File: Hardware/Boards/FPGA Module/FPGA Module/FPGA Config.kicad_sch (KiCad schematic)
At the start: 37 parts, among them Q1 IRLML6244, SW2 RST, SW3 SW_DIP_x03, U1 XCKU3P-FFVA676, U11 MT25QUxxxxxx1xW7, U19 MAX6070BAUT12V+T

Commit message: Completed FPGA module PCB layout
Started PCB routing
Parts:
- C119: renamed from C42; value 4.7uF -> 100nF; footprint Capacitor_SMD:C_0402_1005Metric -> Capacitor_SMD:C_0201_0603Metric
- C120: renamed from C56; footprint Capacitor_SMD:C_0402_1005Metric -> Capacitor_SMD:C_0201_0603Metric
- C121: renamed from C43; footprint Capacitor_SMD:C_0402_1005Metric -> Capacitor_SMD:C_0201_0603Metric
- C122: renamed from C44; footprint Capacitor_SMD:C_0402_1005Metric -> Capacitor_SMD:C_0201_0603Metric
- C123: renamed from C45; footprint Capacitor_SMD:C_0402_1005Metric -> Capacitor_SMD:C_0201_0603Metric
- C124: renamed from C57; footprint Capacitor_SMD:C_0402_1005Metric -> Capacitor_SMD:C_0201_0603Metric
- FB1: footprint (none) -> Inductor_SMD:L_0201_0603Metric
- FB2: renamed from FB3; footprint (none) -> Inductor_SMD:L_0201_0603Metric
- FB3: renamed from FB4; footprint (none) -> Inductor_SMD:L_0201_0603Metric
- R108: renamed from R25; footprint Resistor_SMD:R_0402_1005Metric -> Resistor_SMD:R_0201_0603Metric
- R109: renamed from R26; footprint Resistor_SMD:R_0402_1005Metric -> Resistor_SMD:R_0201_0603Metric
- R110: renamed from R27; footprint Resistor_SMD:R_0402_1005Metric -> Resistor_SMD:R_0201_0603Metric
- R111: renamed from R28; footprint Resistor_SMD:R_0402_1005Metric -> Resistor_SMD:R_0201_0603Metric
- R112: renamed from R51; footprint Resistor_SMD:R_0402_1005Metric -> Resistor_SMD:R_0201_0603Metric
- R113: renamed from R50; footprint Resistor_SMD:R_0402_1005Metric -> Resistor_SMD:R_0201_0603Metric
- R114: renamed from R49; footprint Resistor_SMD:R_0402_1005Metric -> Resistor_SMD:R_0201_0603Metric
- R115: renamed from R58; footprint Resistor_SMD:R_0402_1005Metric -> Resistor_SMD:R_0201_0603Metric
- R116: renamed from R59; footprint Resistor_SMD:R_0402_1005Metric -> Resistor_SMD:R_0201_0603Metric
- R117: renamed from R60; footprint Resistor_SMD:R_0402_1005Metric -> Resistor_SMD:R_0201_0603Metric
- R118: renamed from R52; footprint Resistor_SMD:R_0402_1005Metric -> Resistor_SMD:R_0201_0603Metric
- R119: renamed from R81; footprint Resistor_SMD:R_0402_1005Metric -> Resistor_SMD:R_0201_0603Metric
- R120: renamed from R57; footprint Resistor_SMD:R_0402_1005Metric -> Resistor_SMD:R_0201_0603Metric
- R121: renamed from R53; footprint Resistor_SMD:R_0402_1005Metric -> Resistor_SMD:R_0201_0603Metric
- R122: renamed from R55; footprint Resistor_SMD:R_0402_1005Metric -> Resistor_SMD:R_0201_0603Metric
- R123: renamed from R61; footprint Resistor_SMD:R_0402_1005Metric -> Resistor_SMD:R_0201_0603Metric; now fitted
- R124: renamed from R54; footprint Resistor_SMD:R_0402_1005Metric -> Resistor_SMD:R_0201_0603Metric; now fitted
- R125: renamed from R56; footprint Resistor_SMD:R_0402_1005Metric -> Resistor_SMD:R_0201_0603Metric; now fitted
- R126: renamed from R62; footprint Resistor_SMD:R_0402_1005Metric -> Resistor_SMD:R_0201_0603Metric
- renumbered D8 to D12, Q1 to Q10, TP46 to TP50, TP47 to TP51, U11 to U20, U19 to U21
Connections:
- net FPGA_VREF_N: now also C122.2
- net GND: no longer C119.2, C122.2
- net GNDADC: now reaches FB2.1, U1.N11 (GNDADC)
- net GNDADC: now also C119.2
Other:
- moved on the sheet: C122, FB2

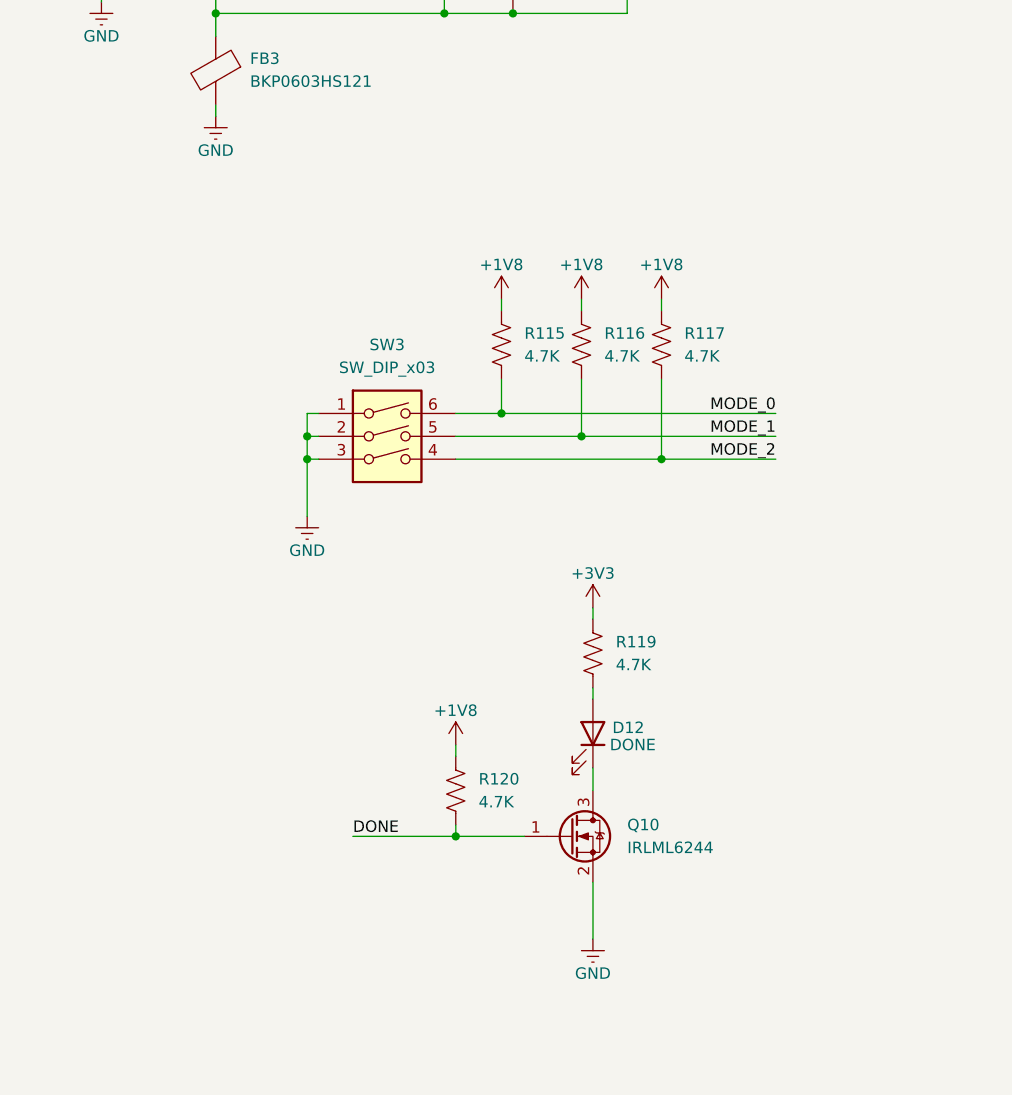
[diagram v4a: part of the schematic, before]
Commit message: Updated SCH and Layout
Added temp sensors for DCDC's, Added MCU control for FPGA mode, removed mode DIP switch
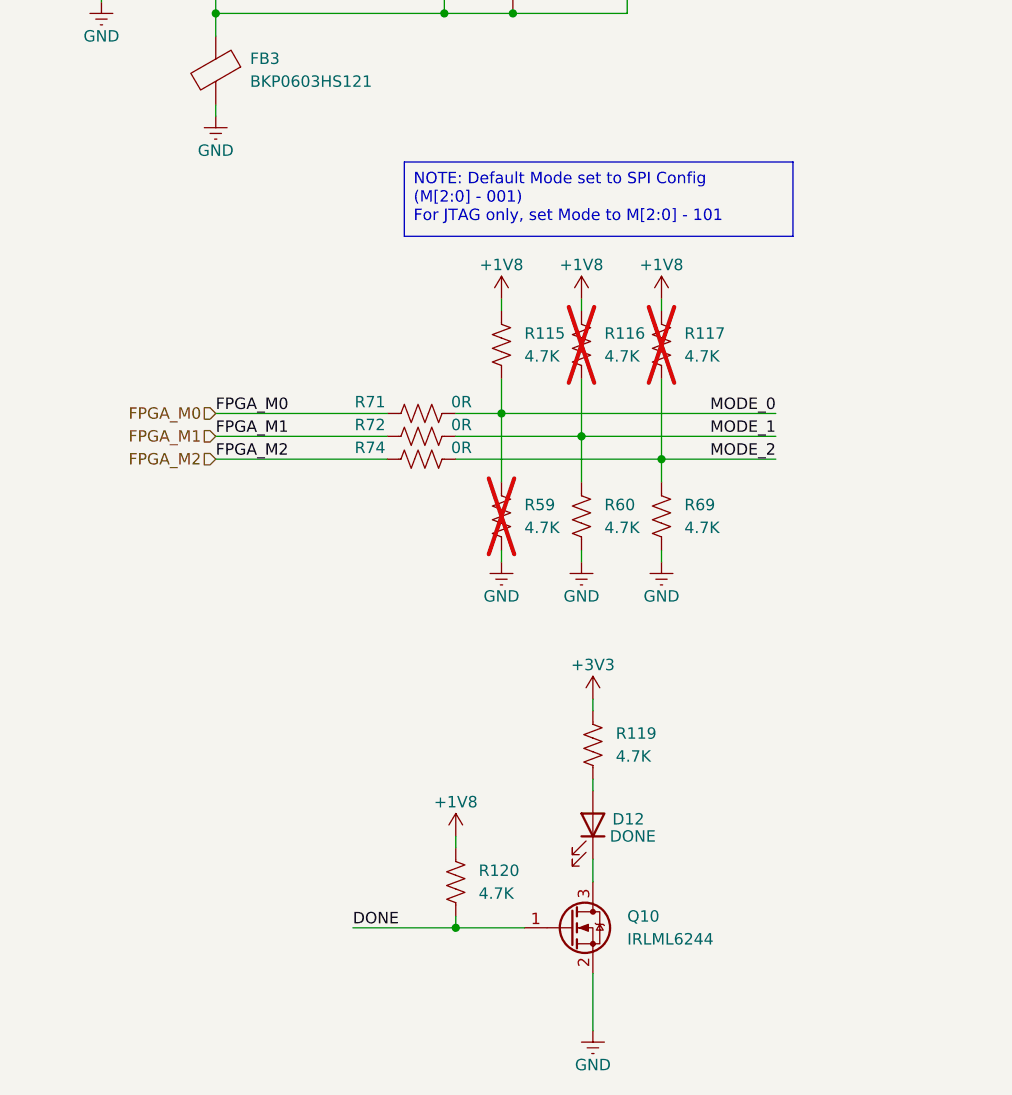
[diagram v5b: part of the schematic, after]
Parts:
- removed SW3: SW_DIP_x03, Button_Switch_SMD:SW_DIP_SPSTx03_Slide_KingTek_DSHP03TJ_W5.25mm_P1.27mm_JPin, symbol Switch:SW_DIP_x03
- added R59, R60, R69: 4.7K, Resistor_SMD:R_0201_0603Metric, symbol Device:R_US
- added R71, R72, R74: 0R, Resistor_SMD:R_0201_0603Metric, symbol Device:R_US
- R116, R117: now not fitted
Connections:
- net GND: now also R59.1, R60.1, R69.1
- net MODE_0: now also R59.2, R71.1
- net MODE_1: now also R60.2, R72.1
- net MODE_2: now also R69.2, R74.1
- new net FPGA_M0: R71.2
- new net FPGA_M1: R72.2
- new net FPGA_M2: R74.2
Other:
- moved on the sheet: D12, Q10, R119, R120

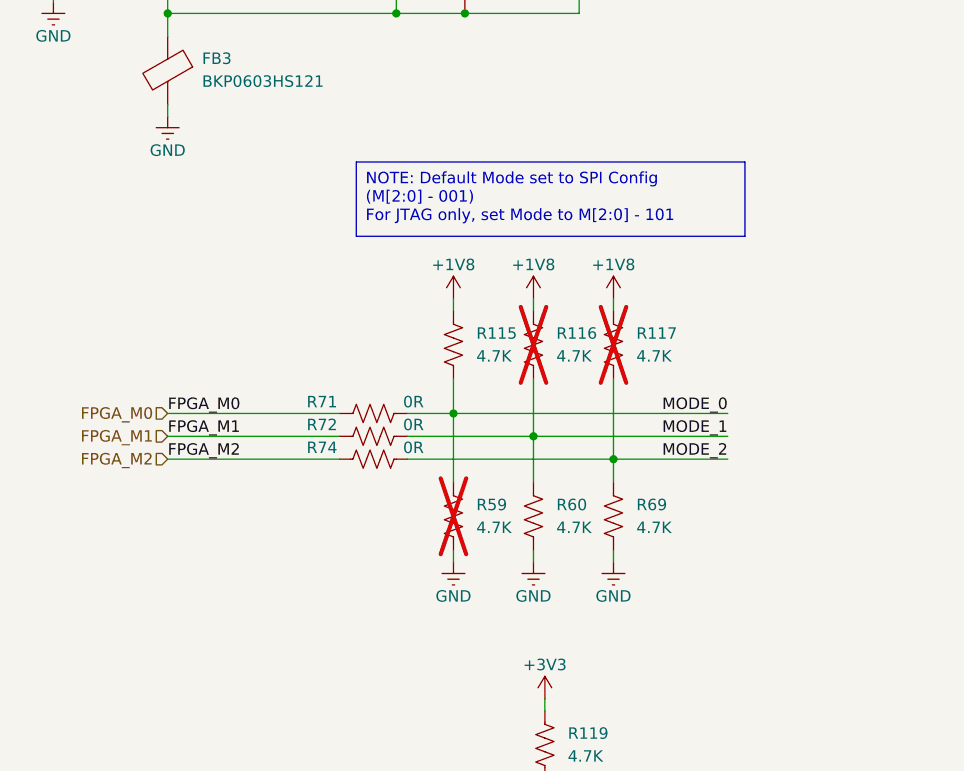
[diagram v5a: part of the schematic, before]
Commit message: FPGA Layout update
Added power panes & moved IO Buffer to MCU
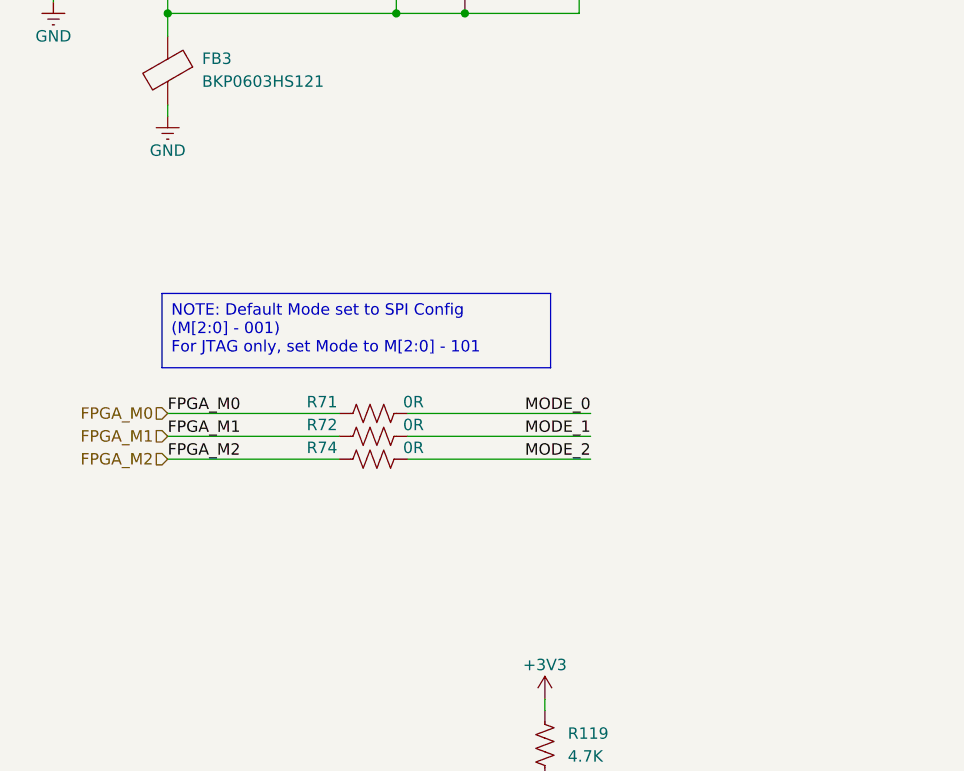
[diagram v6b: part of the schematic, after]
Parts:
- removed R115, R116, R117, R59, R60, R69: 4.7K, Resistor_SMD:R_0201_0603Metric, symbol Device:R_US

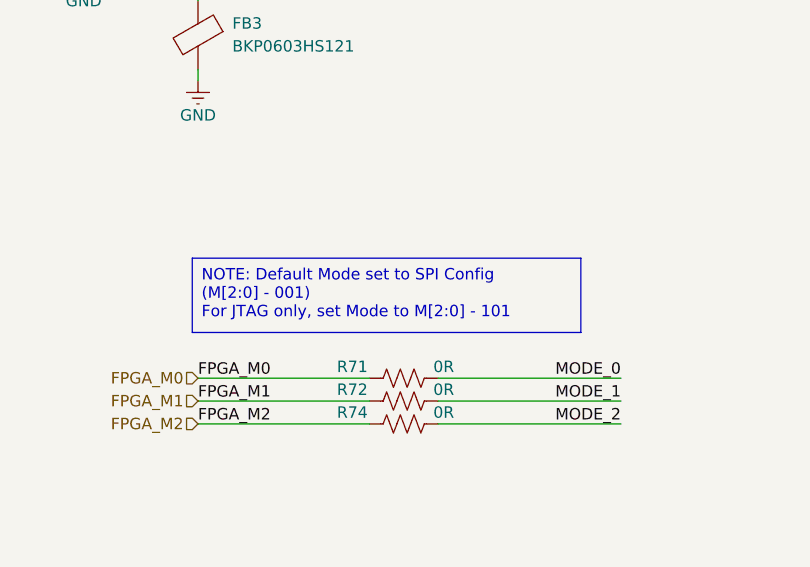
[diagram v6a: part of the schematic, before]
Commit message: Fixed FPGA Module Routing
Reversed B2B headers and re-routed connections to FPGA
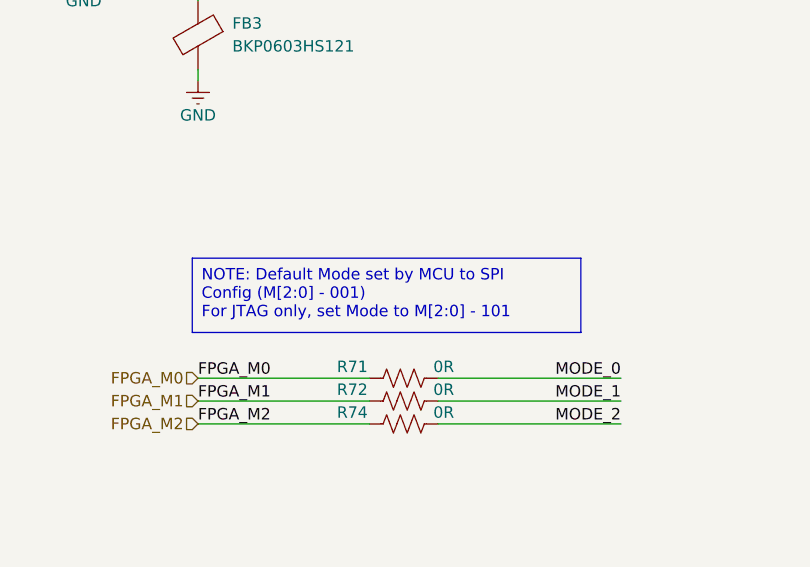
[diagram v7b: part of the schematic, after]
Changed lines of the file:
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@@
 		)
 	)
-	(text_box "NOTE: Default Mode set to SPI Config (M[2:0] - 001)\nFor JTAG only, set Mode to M[2:0] - 101"
+	(text_box "NOTE: Default Mode set by MCU to SPI Config (M[2:0] - 001)\nFor JTAG only, set Mode to M[2:0] - 101"
 		(exclude_from_sim no)
 		(at 92.075 159.385 0)

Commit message: Generated FPGA module gerbers
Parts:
- TP50, TP51: footprint FPGA Module:Test Point 0.75mm -> FPGA Module:Test Point 0.5mm No Silk
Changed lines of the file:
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@@
 			)
 		)
-		(property "Footprint" "FPGA Module:Test Point 0.75mm"
+		(property "Footprint" "FPGA Module:Test Point 0.5mm No Silk"
 			(at 130.81 113.03 0)
 			(effects
@@
 			)
 		)
-		(property "Footprint" "FPGA Module:Test Point 0.75mm"
+		(property "Footprint" "FPGA Module:Test Point 0.5mm No Silk"
 			(at 130.81 128.27 0)
 			(effects
